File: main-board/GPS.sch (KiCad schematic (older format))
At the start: 0 parts

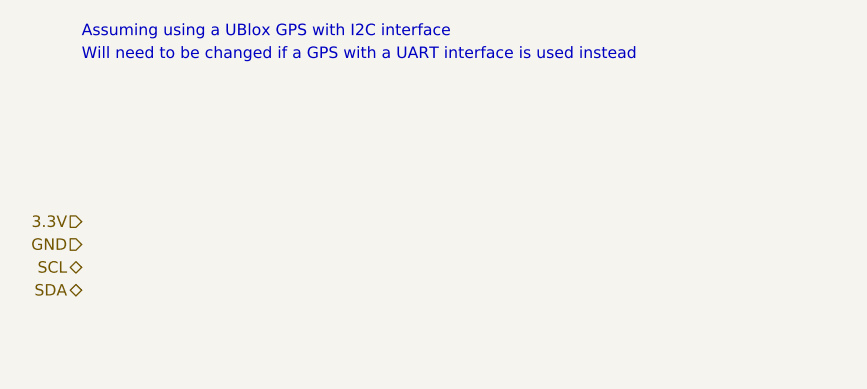
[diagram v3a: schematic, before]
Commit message: More subsheets
Added gps and LED ring
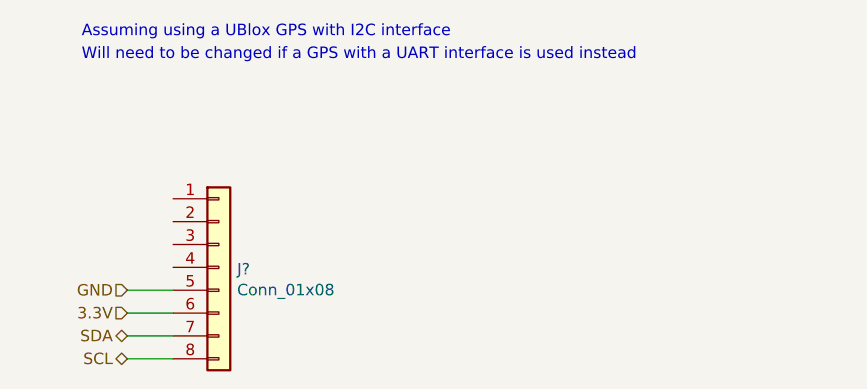
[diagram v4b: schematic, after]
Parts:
- added J?: Conn_01x08, symbol Connector_Generic:Conn_01x08
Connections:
- net 3.3V: now also J?.6 (Pin_6)
- net GND: now also J?.5 (Pin_5)
- net SCL: now also J?.8 (Pin_8)
- net SDA: now also J?.7 (Pin_7)
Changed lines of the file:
@@
 Text Notes 3800 1700 0    50   ~ 0
 Will need to be changed if a GPS with a UART interface is used instead
-Text HLabel 3800 2400 0    50   Input ~ 0
+Text HLabel 4000 2800 0    50   Input ~ 0
 3.3V
-Text HLabel 3800 2500 0    50   Input ~ 0
+Text HLabel 4000 2700 0    50   Input ~ 0
 GND
-Text HLabel 3800 2600 0    50   BiDi ~ 0
+Text HLabel 4000 3000 0    50   BiDi ~ 0
 SCL
-Text HLabel 3800 2700 0    50   BiDi ~ 0
+Text HLabel 4000 2900 0    50   BiDi ~ 0
 SDA
+$Comp
+L Connector_Generic:Conn_01x08 J?
+U 1 1 60AFC3EE
+P 4400 2600
+F 0 "J?" H 4480 2592 50  0000 L CNN
+F 1 "Conn_01x08" H 4480 2501 50  0000 L CNN
+F 2 "" H 4400 2600 50  0001 C CNN
+F 3 "~" H 4400 2600 50  0001 C CNN
+	1    4400 2600
+	1    0    0    -1
+$EndComp
+Wire Wire Line
+	4200 3000 4000 3000
+Wire Wire Line
+	4200 2900 4000 2900
+Wire Wire Line
+	4200 2800 4000 2800
+Wire Wire Line
+	4200 2700 4000 2700
 $EndSCHEMATC
